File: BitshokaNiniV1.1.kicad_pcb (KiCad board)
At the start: 4 copper layers, 56.5 x 99.8 mm, 169 parts, among them J1 54-00164, J2 TC2030-IDC, J3 Conn_01x04, J4 Conn_01x06, J5 USB_C_Receptacle_USB2.0, J6 Conn_01x04, J7 Conn_01x04, Q1 MMBT3906, Q3 MMBT3906, Q4 MMBT2222A, SW1 GT-TC029B-H025-L1N, SW2 GT-TC029B-H025-L1N, T1 net-tie, U10 EMC2101, U2 TPS546D24ARVFR, U23 LM358, U3 RT9080-33GJ5, U4 ESP32-S3-WROOM-1, U5 SPX3819M5-L-1-8, U7 24MHz, U8 KF1950, U9 SN74AVC4T774

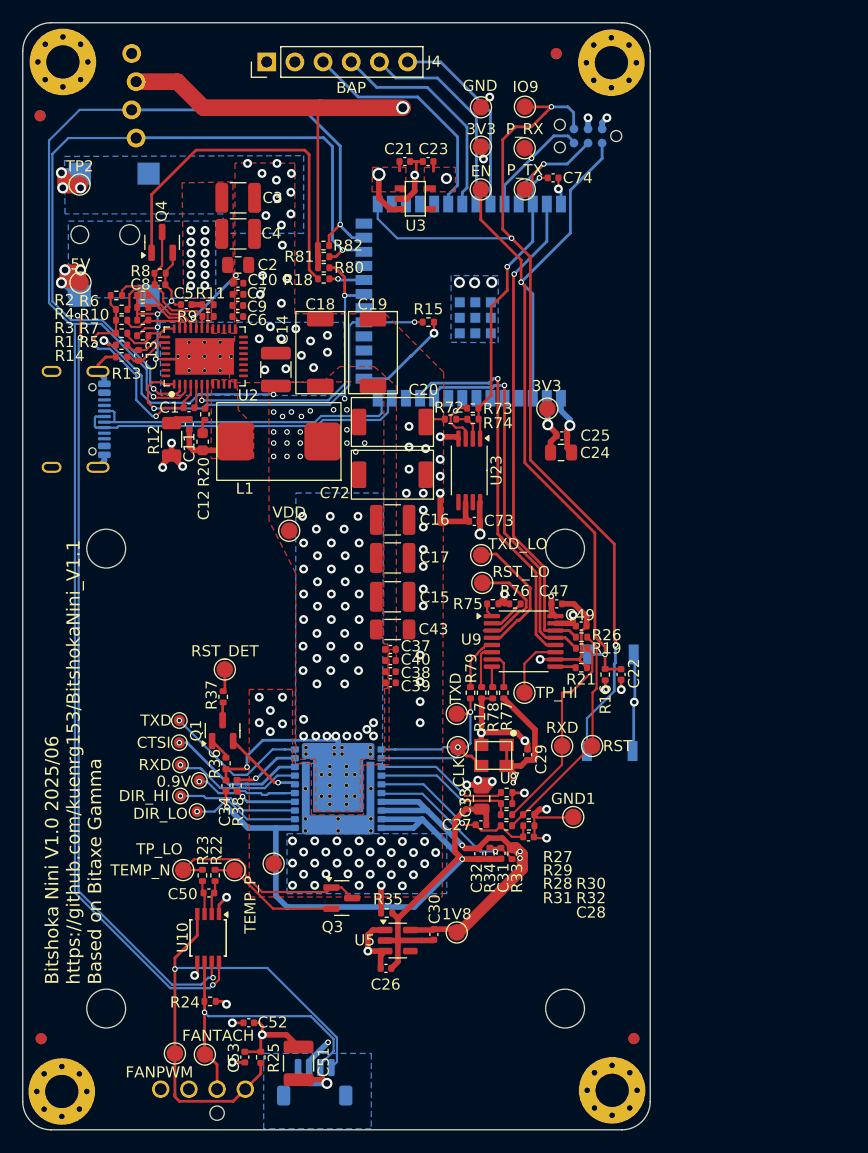
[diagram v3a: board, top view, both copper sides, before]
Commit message: Manfacturing prep
Add part numbers and did initial BOM optimization (Hope to do more after testing)
Created Manufacturing files
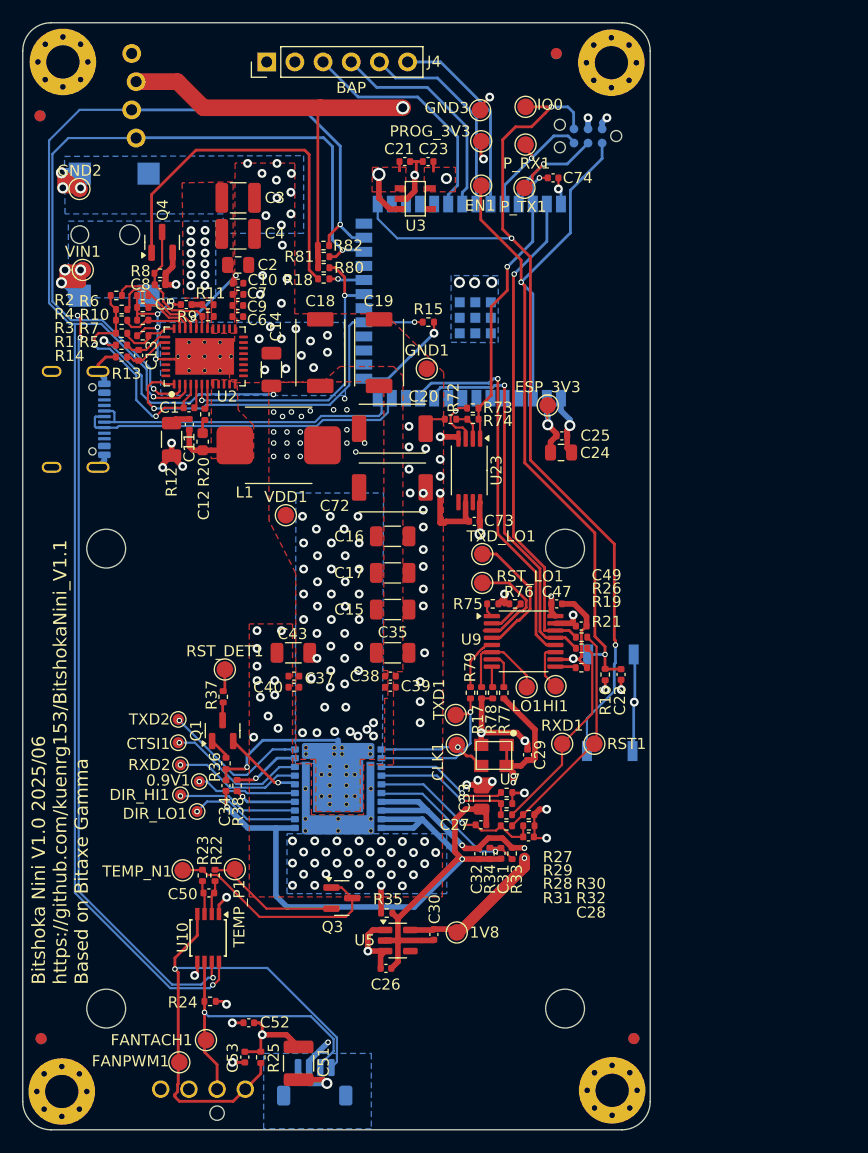
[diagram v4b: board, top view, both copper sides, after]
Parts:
- removed 0.9V, CTSI, DIR_HI, DIR_LO, RXD, TXD: TestPoint, TestPoint:TestPoint_Pad_D1.0mm
- removed 3V3 (x2), 5V, CLK, EN, FANPWM, FANTACH, GND, IO9, P_RX, P_TX, RST, RST_DET, RST_LO, RXD, TEMP_N, TEMP_P, TP2, TP_HI, TP_LO, TXD, TXD_LO, VDD: TestPoint, TestPoint:TestPoint_Pad_D1.5mm
- added 0.9V1: TestPoint, TestPoint:TestPoint_Pad_D1.0mm, F.Cu at (93.1, 115.9)
- added C35: 100uF, Capacitor_SMD:C_1206_3216Metric, F.Cu at (110.5, 104.3)
- added CLK1: TestPoint, TestPoint:TestPoint_Pad_D1.5mm, F.Cu at (116.3, 112.6)
- added CTSI1: TestPoint, TestPoint:TestPoint_Pad_D1.0mm, F.Cu at (91.2, 112.4)
- added DIR_HI1: TestPoint, TestPoint:TestPoint_Pad_D1.0mm, F.Cu at (91.4, 117.1)
- added DIR_LO1: TestPoint, TestPoint:TestPoint_Pad_D1.0mm, F.Cu at (92.9, 118.6)
- added EN1: TestPoint, TestPoint:TestPoint_Pad_D1.5mm, F.Cu at (118.5, 62.2)
- added ESP_3V3: TestPoint, TestPoint:TestPoint_Pad_D1.5mm, F.Cu at (124.5, 82.0)
- added FANPWM1: TestPoint, TestPoint:TestPoint_Pad_D1.5mm, F.Cu at (91.3, 141.2)
- added FANTACH1: TestPoint, TestPoint:TestPoint_Pad_D1.5mm, F.Cu at (93.7, 139.2)
- added GND2: TestPoint, TestPoint:TestPoint_Pad_D1.5mm, F.Cu at (82.3, 62.5)
- added GND3: TestPoint, TestPoint:TestPoint_Pad_D1.5mm, F.Cu at (118.4, 55.4)
- added HI1: TestPoint, TestPoint:TestPoint_Pad_D1.5mm, F.Cu at (125.2, 107.3)
- added IO0: TestPoint, TestPoint:TestPoint_Pad_D1.5mm, F.Cu at (122.5, 55.1)
- added LO1: TestPoint, TestPoint:TestPoint_Pad_D1.5mm, F.Cu at (122.6, 107.4)
- added PROG_3V3: TestPoint, TestPoint:TestPoint_Pad_D1.5mm, F.Cu at (118.5, 58.2)
- added P_RX1: TestPoint, TestPoint:TestPoint_Pad_D1.5mm, F.Cu at (122.5, 58.5)
- added P_TX1: TestPoint, TestPoint:TestPoint_Pad_D1.5mm, F.Cu at (122.4, 62.4)
- added RST1: TestPoint, TestPoint:TestPoint_Pad_D1.5mm, F.Cu at (128.7, 112.5)
- added RST_DET1: TestPoint, TestPoint:TestPoint_Pad_D1.5mm, F.Cu at (95.4, 105.8)
- added RST_LO1: TestPoint, TestPoint:TestPoint_Pad_D1.5mm, F.Cu at (118.6, 98.0)
- added RXD1: TestPoint, TestPoint:TestPoint_Pad_D1.5mm, F.Cu at (125.8, 112.5)
- added RXD2: TestPoint, TestPoint:TestPoint_Pad_D1.0mm, F.Cu at (91.4, 114.4)
- added TEMP_N1: TestPoint, TestPoint:TestPoint_Pad_D1.5mm, F.Cu at (91.6, 123.9)
- added TEMP_P1: TestPoint, TestPoint:TestPoint_Pad_D1.5mm, F.Cu at (96.3, 123.8)
- added TXD1: TestPoint, TestPoint:TestPoint_Pad_D1.5mm, F.Cu at (116.2, 109.9)
- added TXD2: TestPoint, TestPoint:TestPoint_Pad_D1.0mm, F.Cu at (91.2, 110.3)
- added TXD_LO1: TestPoint, TestPoint:TestPoint_Pad_D1.5mm, F.Cu at (118.6, 95.4)
- added VDD1: TestPoint, TestPoint:TestPoint_Pad_D1.5mm, F.Cu at (100.9, 91.9)
- added VIN1: TestPoint, TestPoint:TestPoint_Pad_D1.5mm, F.Cu at (82.6, 69.8)
- C14, C15, C16, C17: footprint Capacitor_SMD:C_1210_3225Metric -> Capacitor_SMD:C_1206_3216Metric
- C28: value C_Small -> 0.1uF
- C31: value 0.1uF? -> 0.1uF
- R21: value 20k -> 10k
- R28: value 440 -> 442
- R29: value 550 -> 549
- R30: value 500 -> 499
- R31: value 335 -> 332
- R32: value 400 -> 402
- R74: value 40k -> 40.2k
- R80, R81, R82: value 4.7k -> 4.64k
- U8: value KF1950 -> ~
- moved GND1 42.5 mm to (113.6, 78.7)
- moved C43 9.19 mm to (101.6, 104.3), turned to 180 degrees
- moved C37 9.02 mm to (101.6, 106.4), turned to 180 degrees
- moved C40 9.02 mm to (101.6, 107.4), turned to 180 degrees
- moved C16 1.48 mm to (110.5, 93.8)
- moved C17 1.35 mm to (110.5, 97.1)
- moved C15 1.15 mm to (110.5, 100.4)
- moved C72 1.15 mm to (110.5, 89.4)
- moved C20 0.60 mm to (110.5, 84.1)
- moved C19 0.55 mm to (109.3, 77.2)
- moved C14 0.40 mm to (99.6, 78.8)
- moved C38 0.40 mm to (110.3, 106.4)
- moved C39 0.40 mm to (110.3, 107.4)
- moved L1 0.35 mm to (100.2, 85.6)
- turned C5 to 180 degrees
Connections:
- C5 pad 1: /Power/AGND -> Net-(U2-AVIN)
- C5 pad 2: Net-(U2-AVIN) -> /Power/AGND
- C8 pad 2: /Power/AGND -> GND
- Q4 pad 2: /Power/AGND -> GND
- R8 pad 2: /Power/AGND -> GND
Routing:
- net Net-(U9-A4): track 3.95 -> 9.02 mm
- net /Power/AGND: track 18.9 -> 14.0 mm
- net GND: track 99.4 -> 101.4 mm, vias 111 -> 117
- net Net-(0.9V1-Pad1): track 10.9 -> 9.05 mm
- net Net-(U9-B4): track 5.89 -> 4.33 mm
- net /Fan/TEMP_N: track 19.7 -> 20.6 mm
- net /KF1950/1V8: track 74.1 -> 74.9 mm
- net /VDD: vias 73 -> 72

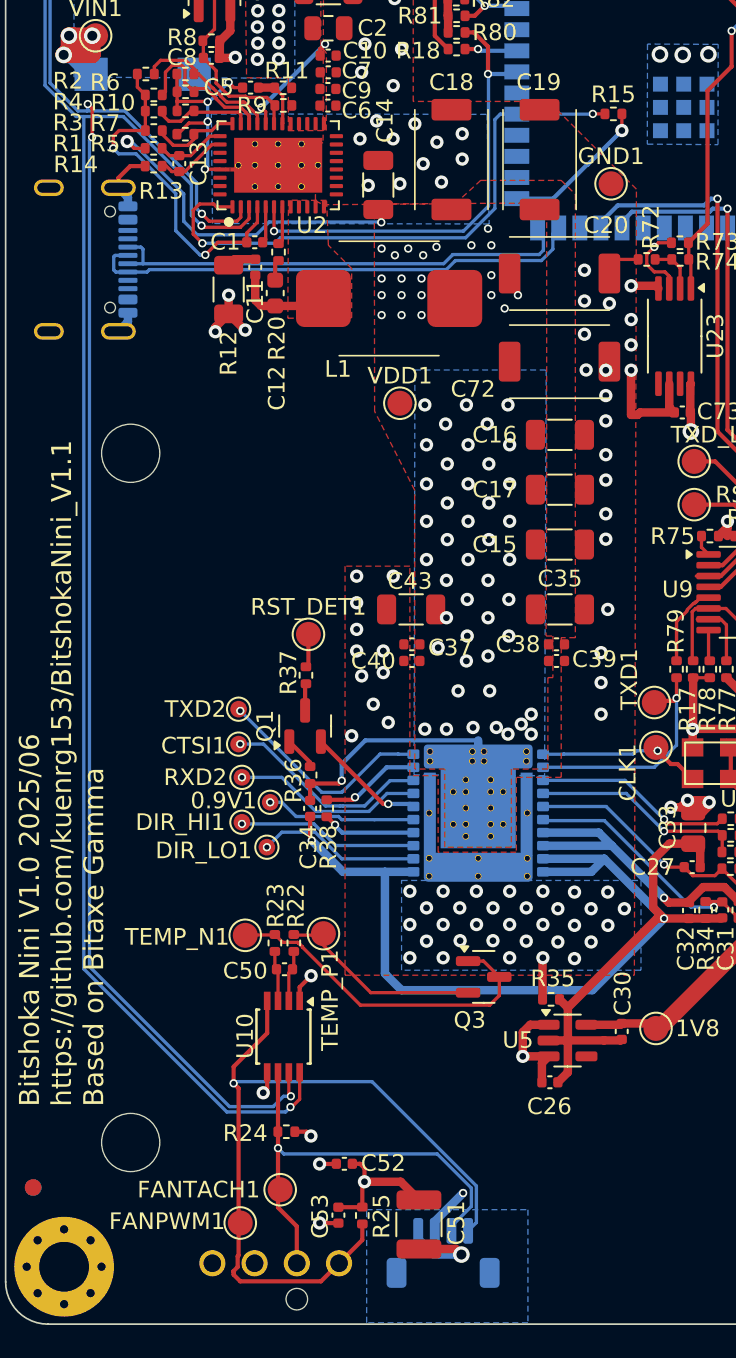
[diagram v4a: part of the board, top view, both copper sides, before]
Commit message: Addressed Bitaxe Gamma Issues
- moved Fan caps
- added USB CC1 & CC2 pulldowns
- (I2C pullups were already done)
- reviewed but so far did not address any of the other issues/bugs
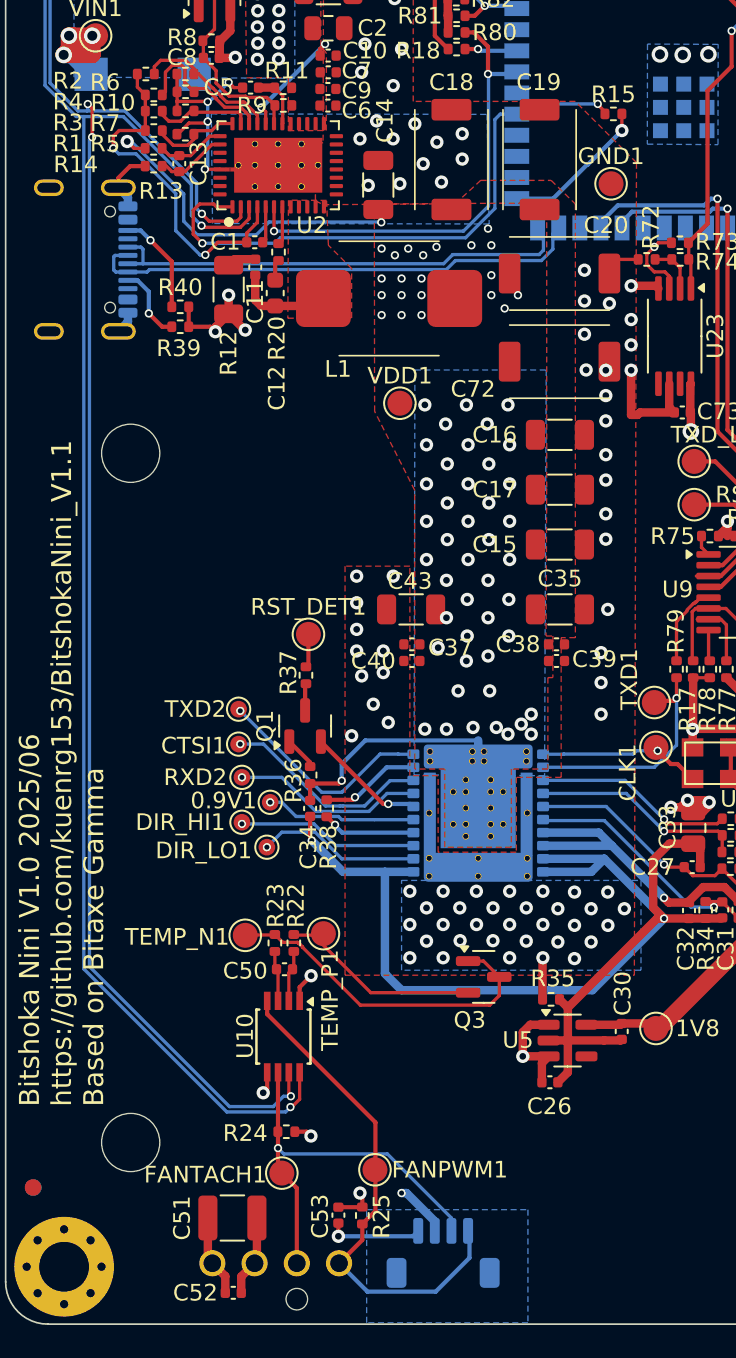
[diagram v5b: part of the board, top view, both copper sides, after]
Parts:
- added R39: 4.64k, Resistor_SMD:R_0402_1005Metric, F.Cu at (87.7, 87.3)
- added R40: 4.64k, Resistor_SMD:R_0402_1005Metric, F.Cu at (87.7, 86.1)
- moved C51 11.2 mm to (90.8, 140.9), turned to 180 degrees
- moved C52 10.2 mm to (90.9, 145.4)
- moved FANPWM1 8.71 mm to (99.4, 138.0)
- moved FANTACH1 1.00 mm to (93.8, 138.2)
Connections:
- J5 pad A5: unconnected-(J5-CC1-PadA5) -> Net-(J5-CC1)
- J5 pad B5: unconnected-(J5-CC2-PadB5) -> Net-(J5-CC2)
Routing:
- net /Fan/FAN_PWM: track 47.7 -> 30.4 mm, vias 1 -> 0
- net /5V: track 194.2 -> 187.6 mm
- net Net-(J5-CC2): track 0.00 -> 6.13 mm, vias 0 -> 1
- net GND: track 101.4 -> 107.1 mm, vias 117 -> 115
- net Net-(J5-CC1): track 0.00 -> 4.66 mm, vias 0 -> 1
- net /Fan/FAN_TACH: track 27.6 -> 24.9 mm
- net /Power/PGOOD: track 35.4 -> 36.0 mm
